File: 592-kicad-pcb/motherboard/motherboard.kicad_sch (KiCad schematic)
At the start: 0 parts

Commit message: add hierarchy demo for clock sources
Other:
- added sheet clock_sources (clock_sources.kicad_sch)
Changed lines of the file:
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@@
 	(generator_version "9.0")
 	(paper "A4")
+	(sheet
+		(at 17.78 16.51)
+		(size 35.56 21.59)
+		(exclude_from_sim no)
+		(in_bom yes)
+		(on_board yes)
+		(dnp no)
+		(fields_autoplaced yes)
+		(stroke
+			(width 0.1524)
+			(type solid)
+		)
+		(fill
+			(color 0 0 0 0.0000)
+		)
+		(property "Sheetname" "clock_sources"
+			(at 17.78 15.7984 0)
+			(effects
+				(font
+					(size 1.27 1.27)
+				)
+				(justify left bottom)
+				(hide yes)
+			)
+		)
+		(property "Sheetfile" "clock_sources.kicad_sch"
+			(at 17.78 38.6846 0)
+			(effects
+				(font
+					(size 1.27 1.27)
+				)
+				(justify left top)
+			)
+		)
+		(instances
+			(project "motherboard"
+				(path "/5b0c97ac-fa03-4db8-b41b-0eee32b6f55d"
+					(page "2")
+				)
+			)
+		)
+	)
 	(sheet_instances
 		(path "/"

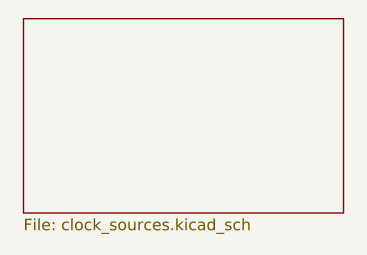
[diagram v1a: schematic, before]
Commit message: add schematic for clock generator, some symbols
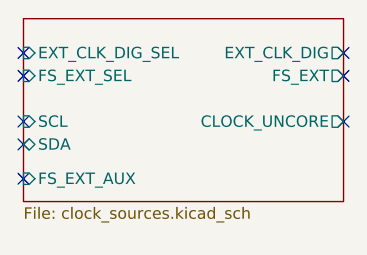
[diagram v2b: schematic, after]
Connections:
- no-connect marks 0 -> 8
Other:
- sheet clock_sources ports: added CLOCK_UNCORE, EXT_CLK_DIG, EXT_CLK_DIG_SEL, FS_EXT, FS_EXT_AUX, FS_EXT_SEL, SCL, SDA; removed none
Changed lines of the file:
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@@
 	(generator_version "9.0")
 	(paper "A4")
+	(no_connect
+		(at 17.78 27.94)
+	)
+	(no_connect
+		(at 53.34 27.94)
+	)
+	(no_connect
+		(at 53.34 20.32)
+	)
+	(no_connect
+		(at 17.78 30.48)
+	)
+	(no_connect
+		(at 17.78 34.29)
+	)
+	(no_connect
+		(at 17.78 20.32)
+	)
+	(no_connect
+		(at 17.78 22.86)
+	)
+	(no_connect
+		(at 53.34 22.86)
+	)
 	(sheet
 		(at 17.78 16.51)
-		(size 35.56 21.59)
+		(size 35.56 20.32)
 		(exclude_from_sim no)
 		(in_bom yes)
@@
 		)
 		(property "Sheetfile" "clock_sources.kicad_sch"
-			(at 17.78 38.6846 0)
+			(at 17.78 37.4146 0)
 			(effects
 				(font
@@
 			)
 		)
+		(pin "SCL" input
+			(at 17.78 27.94 180)
+			(effects
+				(font
+					(size 1.27 1.27)
+				)
+				(justify left)
+			)
+		)
+		(pin "EXT_CLK_DIG_SEL" input
+			(at 17.78 20.32 180)
+			(effects
+				(font
+					(size 1.27 1.27)
+				)
+				(justify left)
+			)
+		)
+		(pin "CLOCK_UNCORE" output
+			(at 53.34 27.94 0)
+			(effects
+				(font
+					(size 1.27 1.27)
+				)
+				(justify right)
+			)
+		)
+		(pin "FS_EXT_SEL" input
+			(at 17.78 22.86 180)
+			(effects
+				(font
+					(size 1.27 1.27)
+				)
+				(justify left)
+			)
+		)
+		(pin "FS_EXT" output
+			(at 53.34 22.86 0)
+			(effects
+				(font
+					(size 1.27 1.27)
+				)
+				(justify right)
+			)
+		)
+		(pin "SDA" bidirectional
+			(at 17.78 30.48 180)
+			(effects
+				(font
+					(size 1.27 1.27)
+				)
+				(justify left)
+			)
+		)
+		(pin "EXT_CLK_DIG" output
+			(at 53.34 20.32 0)
+			(effects
+				(font
+					(size 1.27 1.27)
+				)
+				(justify right)
+			)
+		)
+		(pin "FS_EXT_AUX" input
+			(at 17.78 34.29 180)
+			(effects
+				(font
+					(size 1.27 1.27)
+				)
+				(justify left)
+			)
+		)

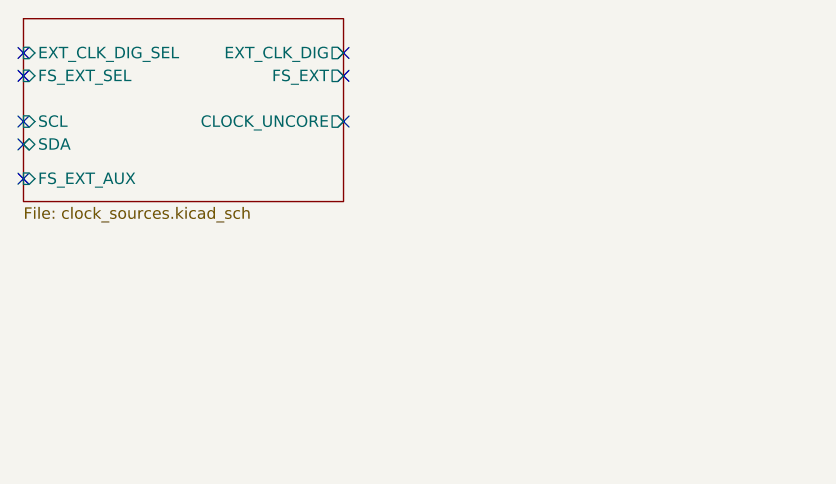
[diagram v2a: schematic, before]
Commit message: update signal supporting ckts
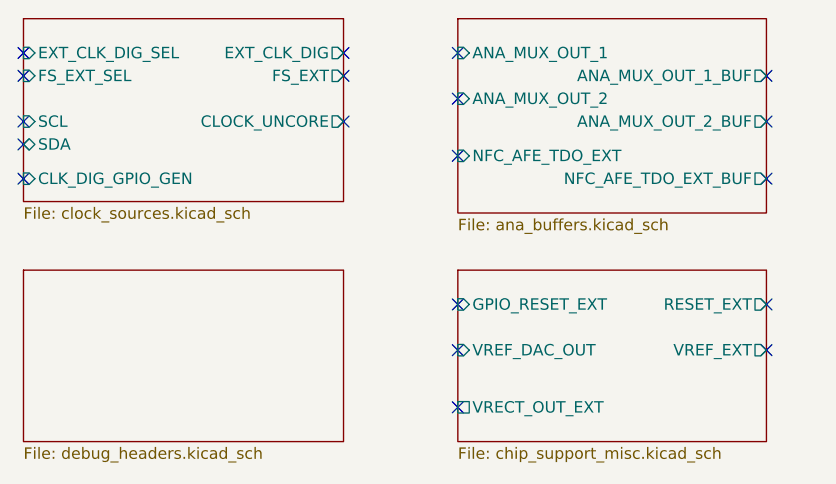
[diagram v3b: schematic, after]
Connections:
- no-connect marks 8 -> 19
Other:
- added sheet ana_buffers (ana_buffers.kicad_sch)
- added sheet chip_support_misc (chip_support_misc.kicad_sch)
- added sheet debug_headers (debug_headers.kicad_sch)
- sheet clock_sources ports: added CLK_DIG_GPIO_GEN; removed FS_EXT_AUX

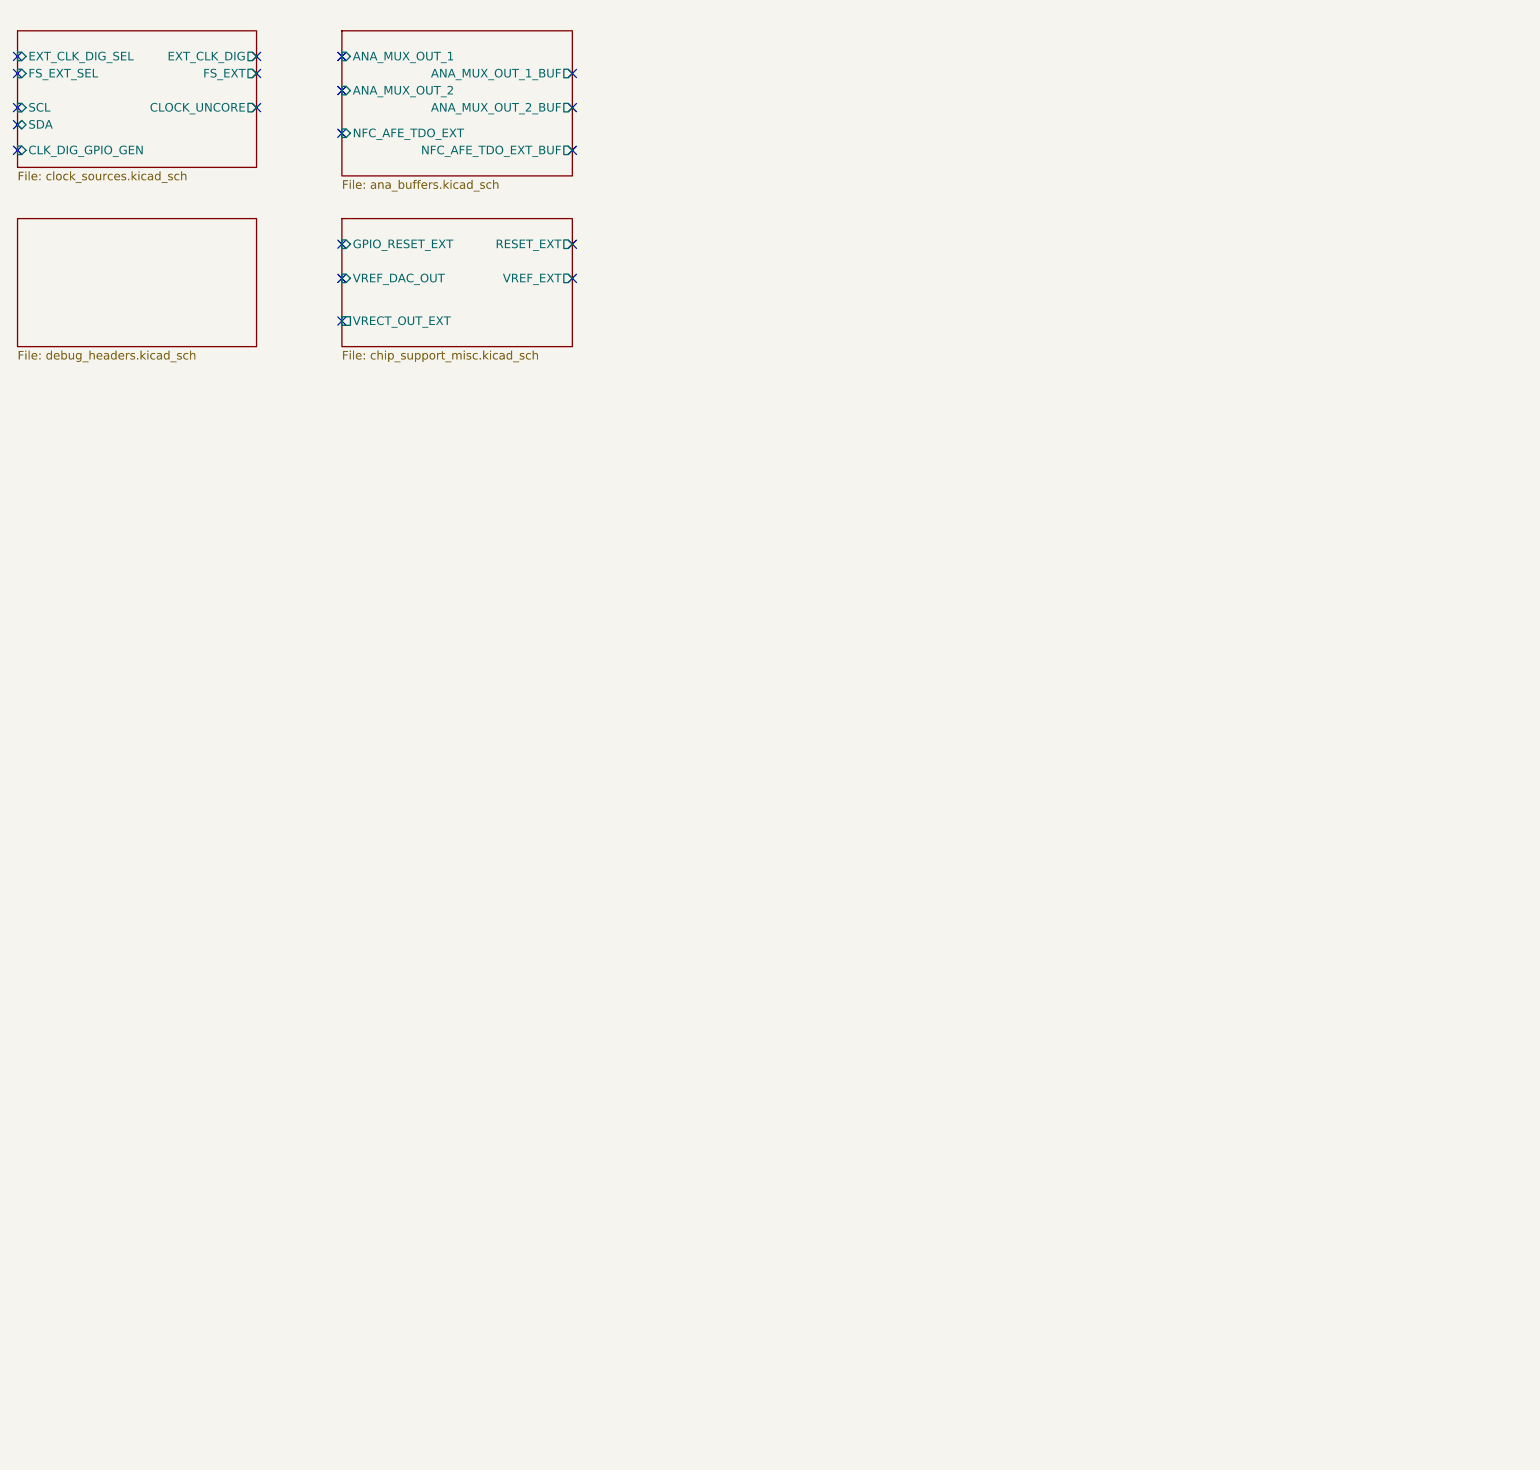
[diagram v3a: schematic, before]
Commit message: clean up supporting blocks; add nucleo symbol
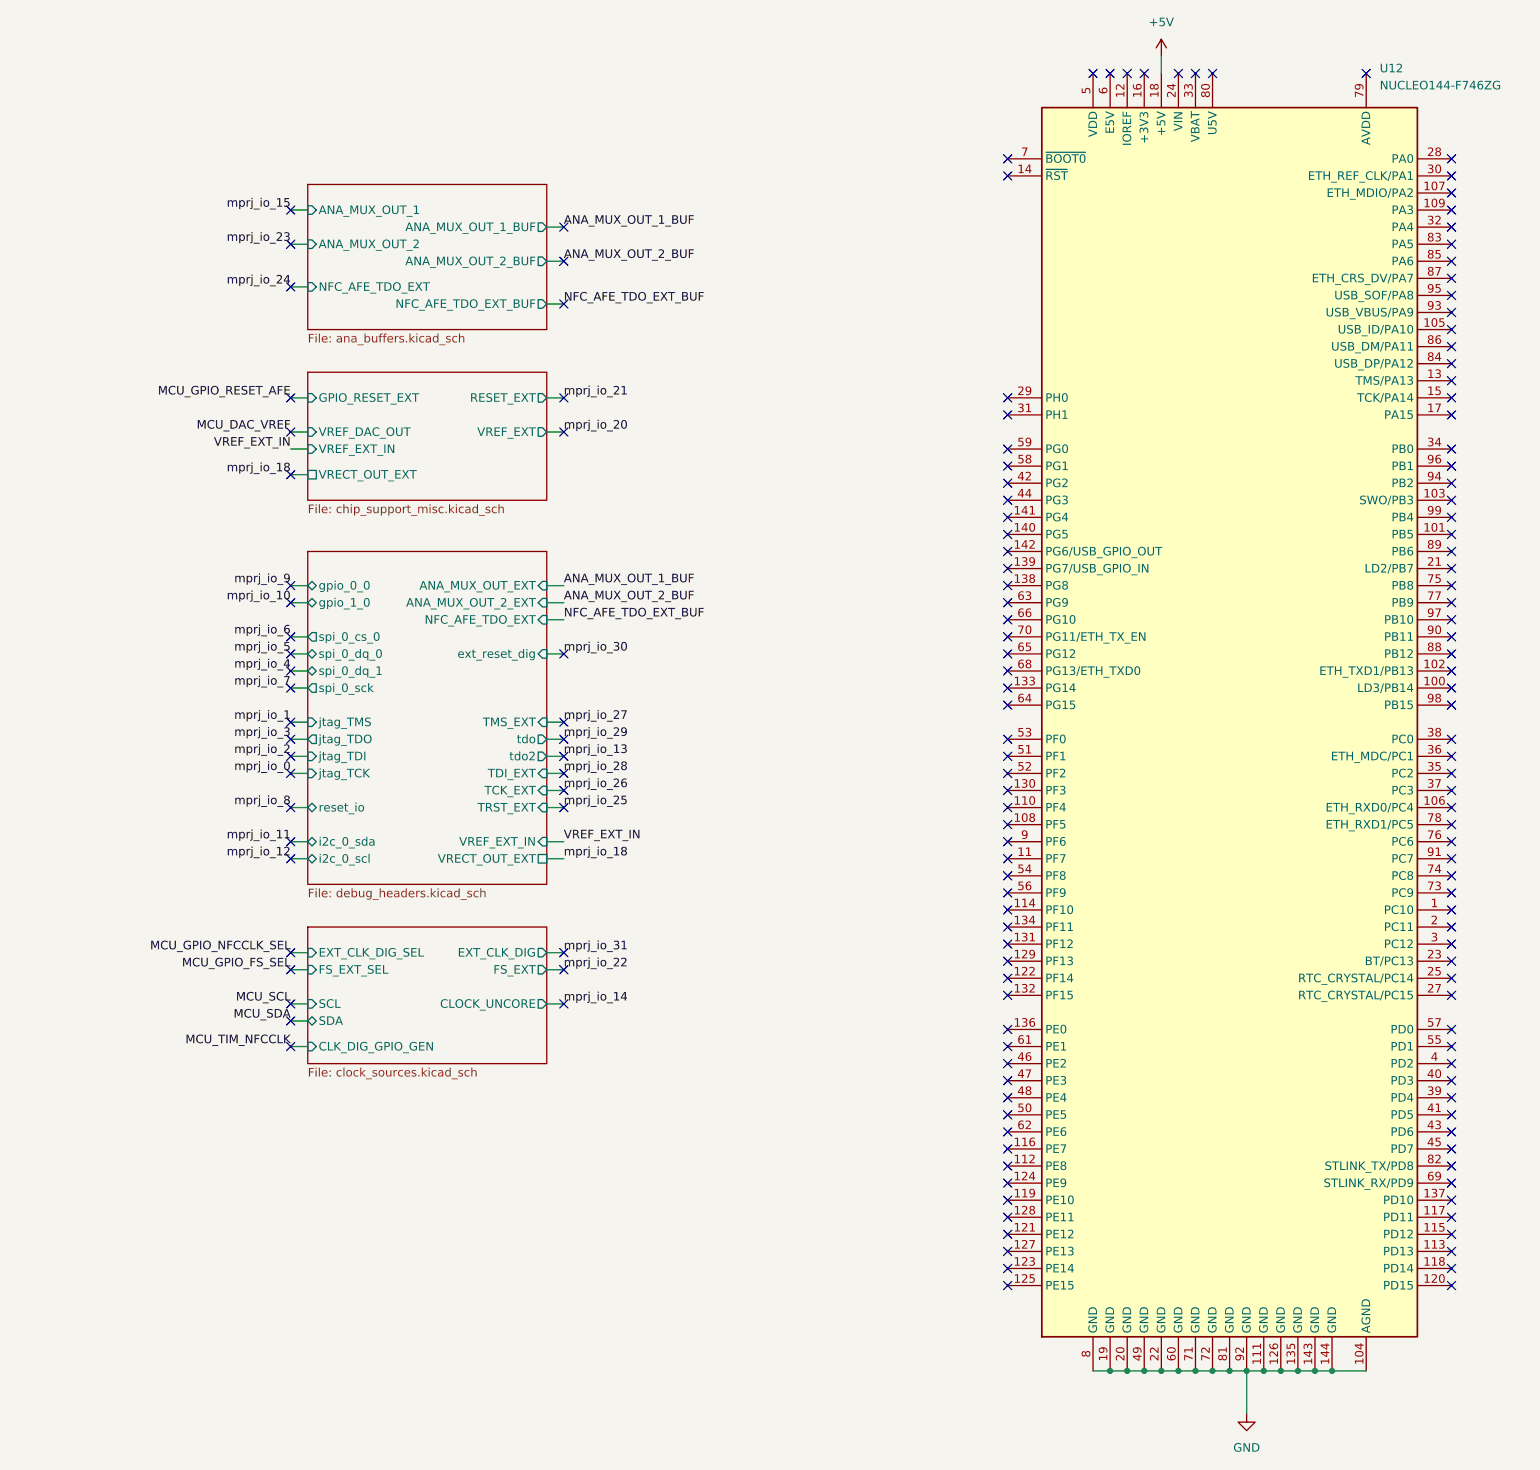
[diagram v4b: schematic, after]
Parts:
- added U12: NUCLEO144-F746ZG, Module:ST_Morpho_Connector_144_STLink, symbol MCU_Module:NUCLEO144-F746ZG
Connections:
- new net +5V: U12.18 (+5V)
- new net GND: U12.104 (AGND), U12.111 (GND), U12.126 (GND), U12.135 (GND), U12.143 (GND), U12.144 (GND), U12.19 (GND), U12.20 (GND), U12.22 (GND), U12.49 (GND), U12.60 (GND), U12.71 (GND), U12.72 (GND), U12.8 (GND), U12.81 (GND), U12.92 (GND)
- no-connect marks 19 -> 163
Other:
- sheet chip_support_misc ports: added VREF_EXT_IN; removed none
- sheet debug_headers ports: added ANA_MUX_OUT_2_EXT, ANA_MUX_OUT_EXT, NFC_AFE_TDO_EXT, TCK_EXT, TDI_EXT, TMS_EXT, TRST_EXT, VRECT_OUT_EXT, VREF_EXT_IN, ext_reset_dig, gpio_0_0, gpio_1_0, i2c_0_scl, i2c_0_sda, jtag_TCK, jtag_TDI, jtag_TDO, jtag_TMS, reset_io, spi_0_cs_0, spi_0_dq_0, spi_0_dq_1, spi_0_sck, tdo, tdo2; removed none
